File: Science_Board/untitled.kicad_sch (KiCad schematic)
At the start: 8 parts, among them Q1 BS250, U1 AP63205WU

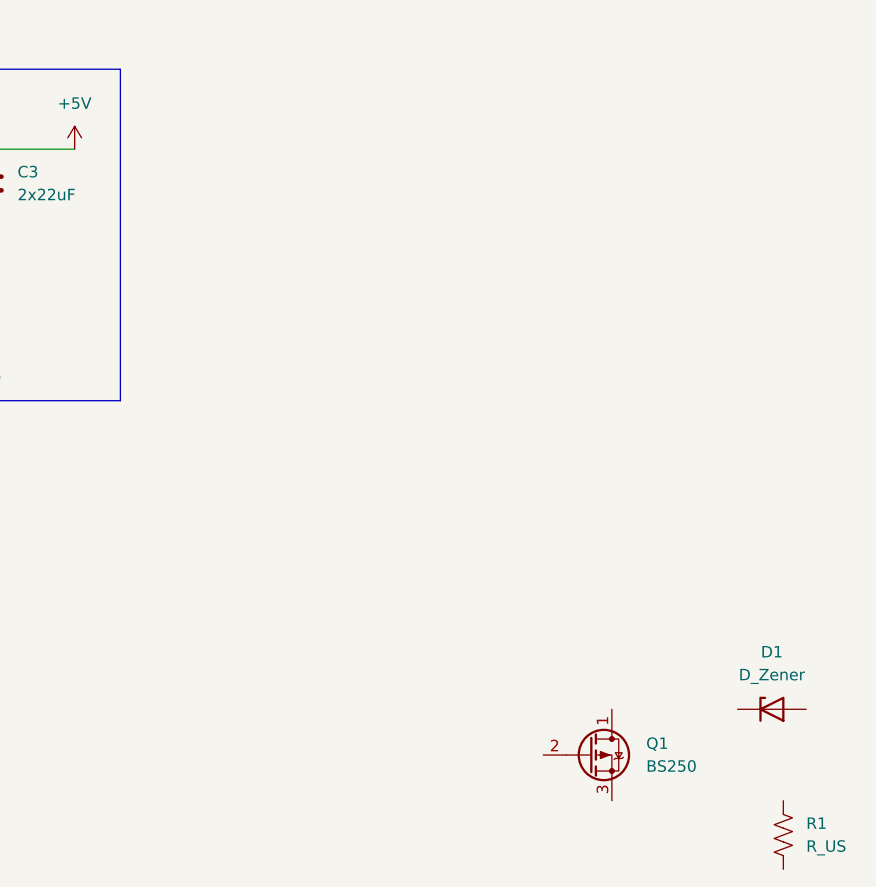
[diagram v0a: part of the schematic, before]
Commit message: Reverse Voltage Protection Complete
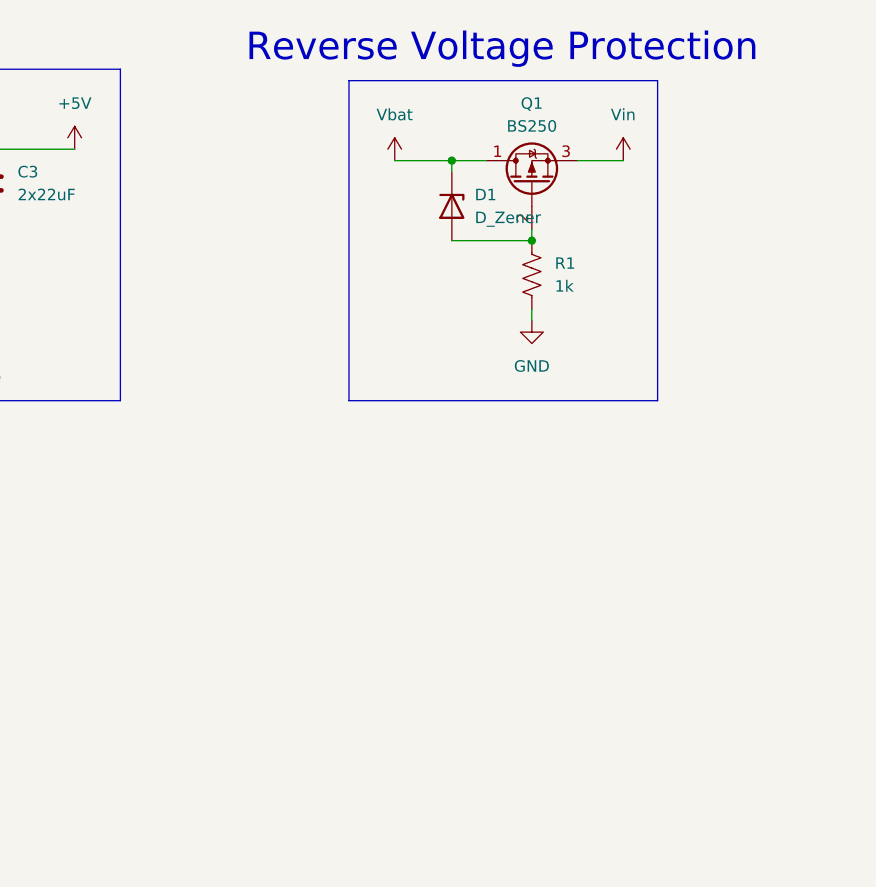
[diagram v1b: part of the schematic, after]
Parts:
- R1: value R_US -> 1k
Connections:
- net GND: now also R1.1
- net Vbat: now also D1.1 (K), Q1.1 (D)
- net at D1.2 (A): now also Q1.2 (G), R1.2
- net Vin: now reaches Q1.3 (S)
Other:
- note added: "Reverse Voltage Protection"
- moved on the sheet: D1, Q1, R1

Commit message: RoveNode
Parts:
- added U2: (no value), MRDT_Shields:RoveNode_H5, symbol MRDT_Shields:RoveNode_H5
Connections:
- net GND: now also U2.2 (GND)
- net Vbat: now also U2.1 (VIN)
- new net +3V3: U2.3 (3V3)
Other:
- note added: "RoveNode"
- moved on the sheet: D1, Q1, R1

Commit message: EFuses
They done
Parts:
- added C4, C5, C6, C7, C8, C9: 1uF, symbol Device:C
- added D5, D6, D7: 24V, Package_DIP:DIP-40_W15.24mm, symbol Device:D_Zener
- added IC1, IC2, IC3: TCKE602RM, TCKE602RM, symbol MRDT_TCKE602RM:TCKE602RM
- added R10, R6, R8: 4.7k, Package_QFP:LQFP-100_14x14mm_P0.5mm, symbol Device:R_US
- added R5, R7, R9: 10k, symbol Device:R_US
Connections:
- net GND: now also C4.2, C5.2, C6.2, C7.2, C8.2, C9.2, D5.2 (A), D6.2 (A), D7.2 (A), IC1.2 (GND_1), IC1.3 (MODE), IC1.5 (GND_2), IC2.2 (GND_1), IC2.3 (MODE), IC2.5 (GND_2), IC3.2 (GND_1), IC3.3 (MODE), IC3.5 (GND_2), R10.2, R6.2, R8.2
- net Vbat: now also C4.1, C6.1, C8.1, D5.1 (K), D6.1 (K), D7.1 (K), IC1.1 (VIN), IC2.1 (VIN), IC3.1 (VIN)
- new net: R7.2, R8.1
- new net: IC3.4 (ILIM), R9.1
- new net: R10.1, R9.2
- new net: IC1.4 (ILIM), R5.1
- new net: IC2.4 (ILIM), R7.1
- new net: R5.2, R6.1
- new net Vaf: C5.1, IC1.6 (VOUT)
- new net Vsm: C7.1, IC2.6 (VOUT)
- new net Vuv: C9.1, IC3.6 (VOUT)
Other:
- note added: "AF EFuse"
- note added: "SM EFuse"
- note added: "UV EFuse"
- moved on the sheet: C1, C2, C3, D1, L1, Q1, R1, U1, U2
